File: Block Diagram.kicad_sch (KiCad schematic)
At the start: 0 parts

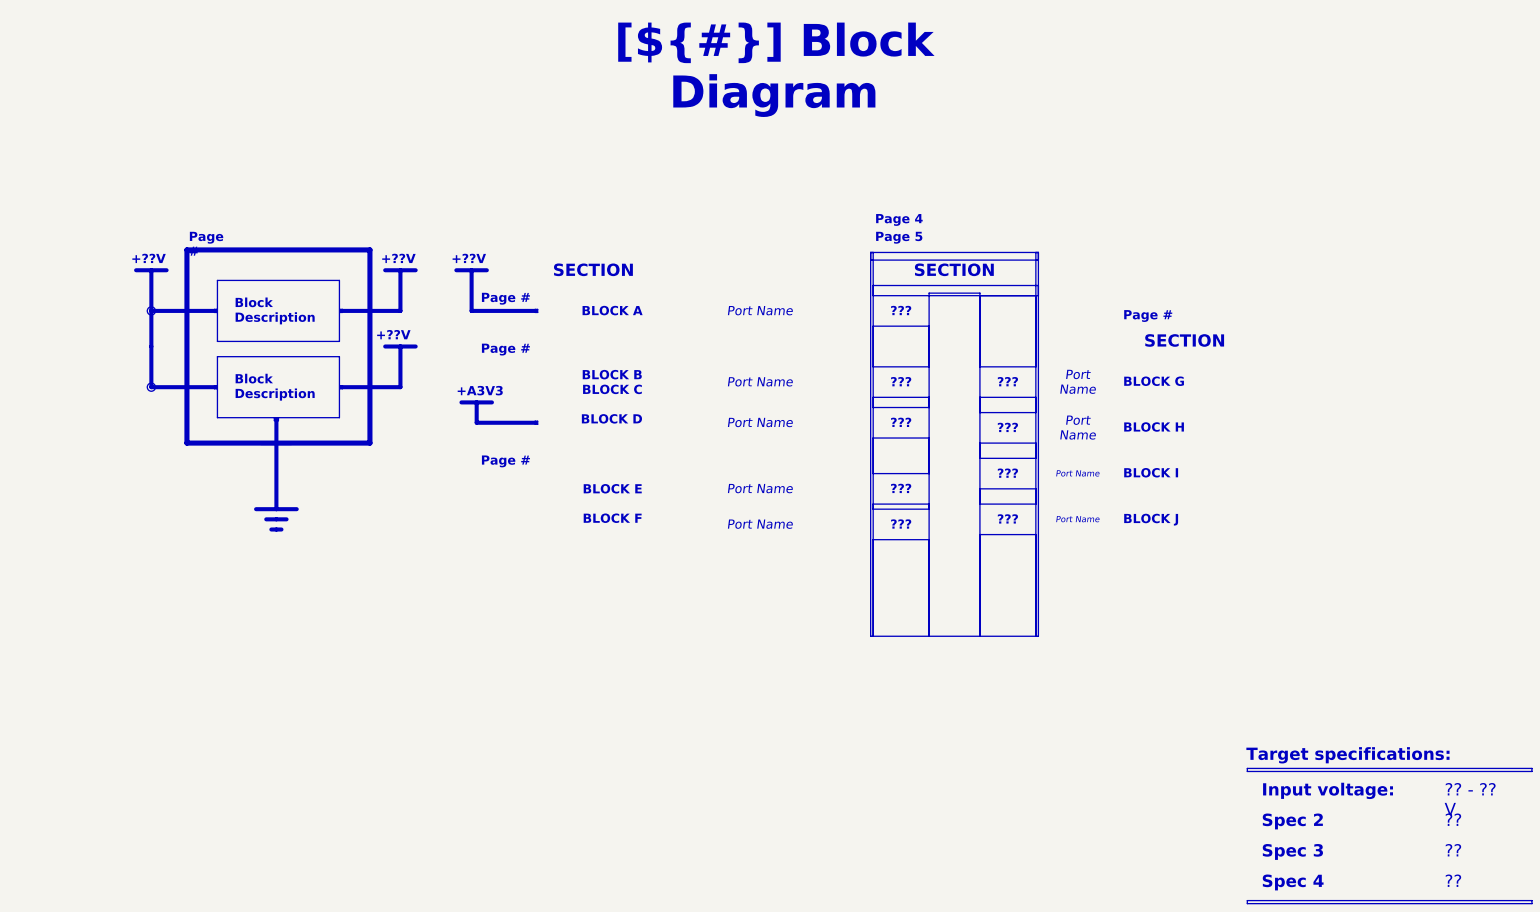
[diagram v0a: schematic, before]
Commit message: PCB[Grounding, Heat]: Added some more pours for heat considerations for bjt, stiched more vias for heat consideration on balanace resistors. SCH[Notes, Block Diagram]: Working on spelling and notes updates, started block diagram.
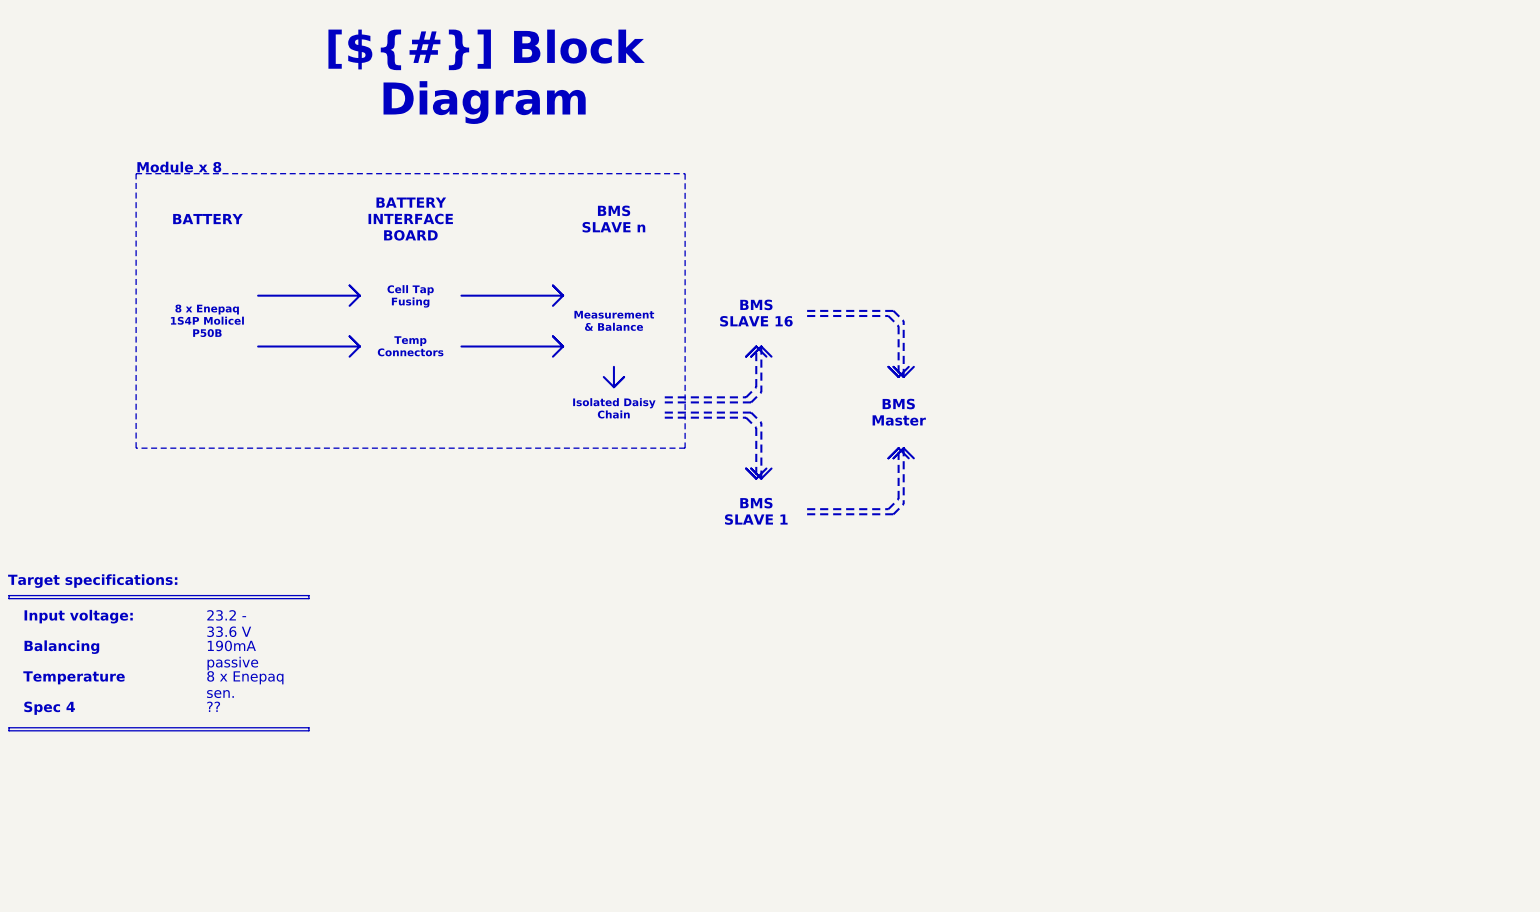
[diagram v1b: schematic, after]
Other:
- note added: "Module x 8"
- note removed: "+??V"
- note removed: "+A3V3"

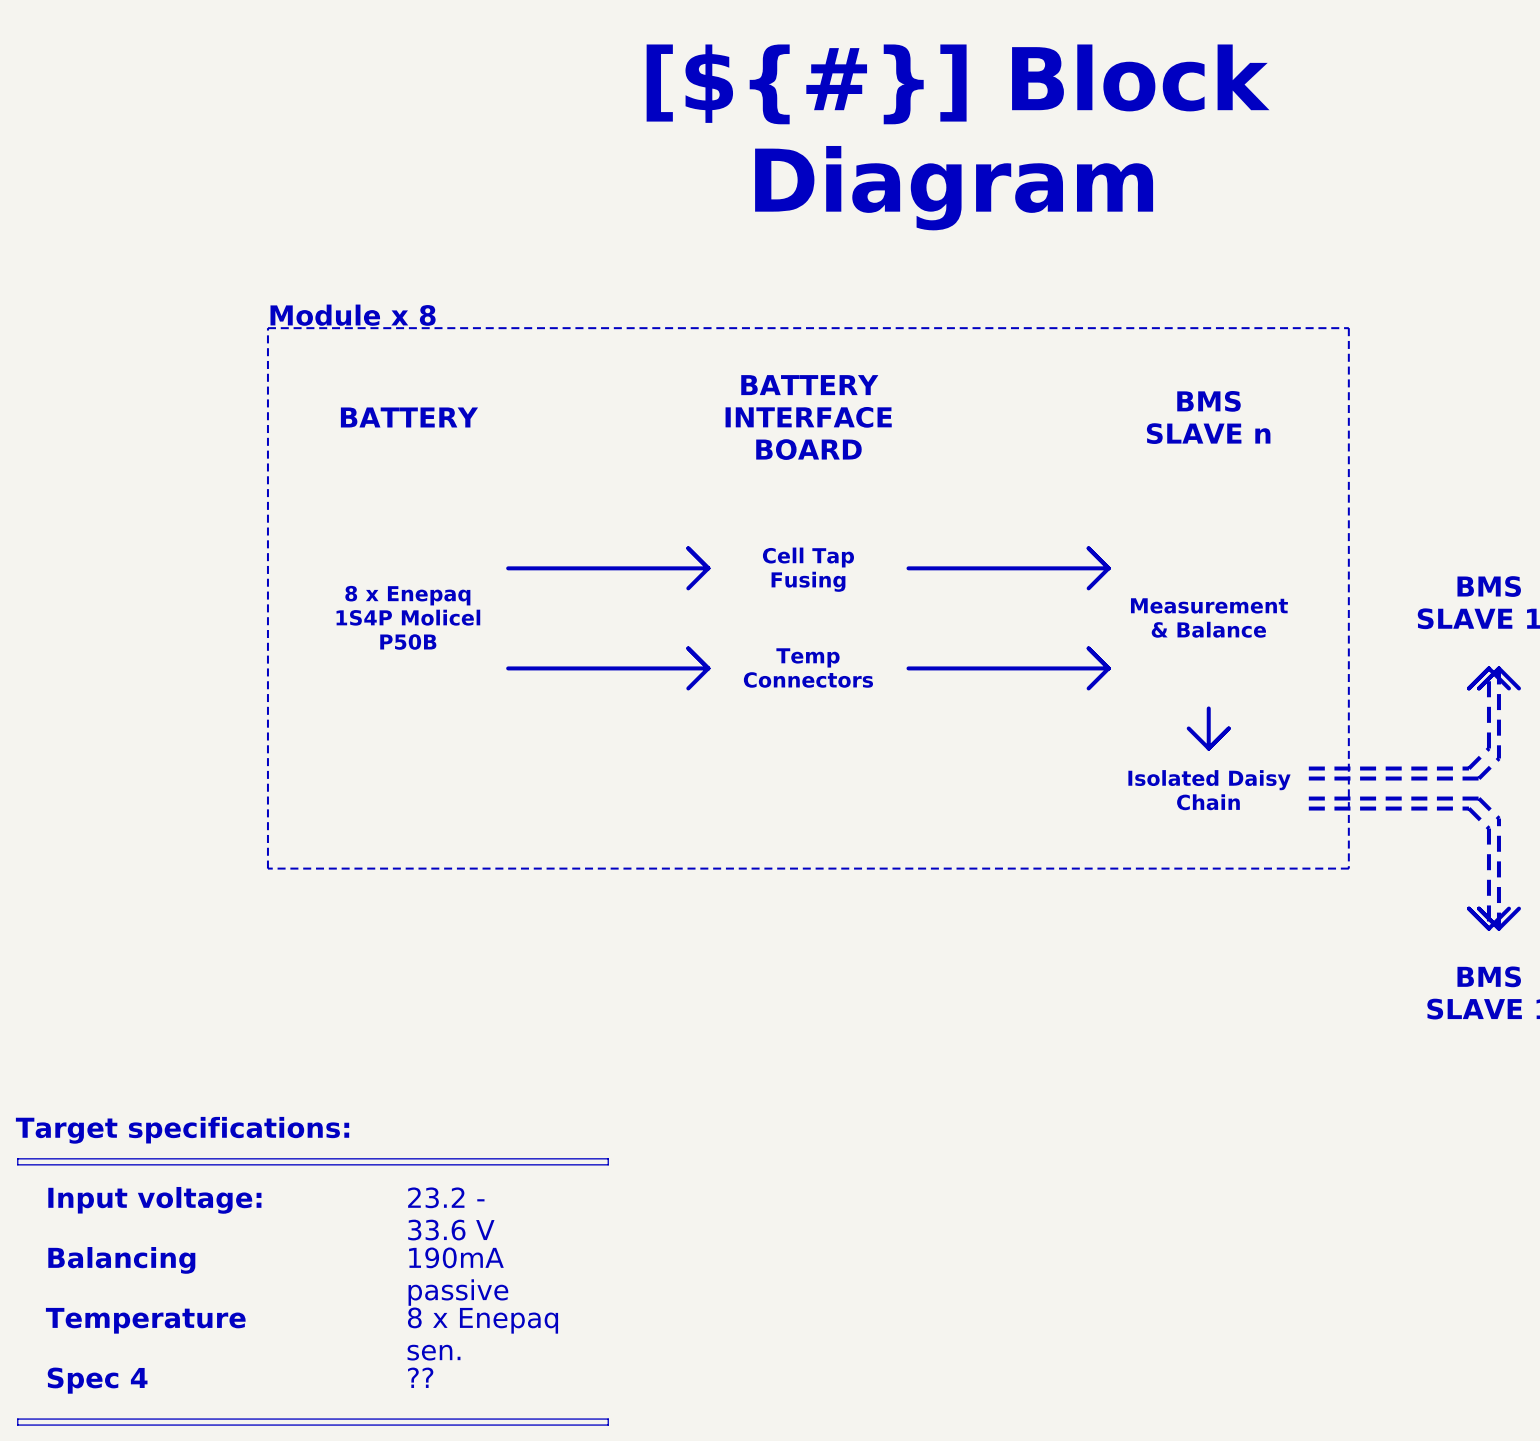
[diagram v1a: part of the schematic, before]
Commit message: PCB[Test Points, Mechanical, Silk]: Finalized Mounting Points, Added Testpoints with adjecent silkscreen labels. SCH[Test Points, Notes]: Added/Updated notes for all pages, cleaned up errors spelling ect.
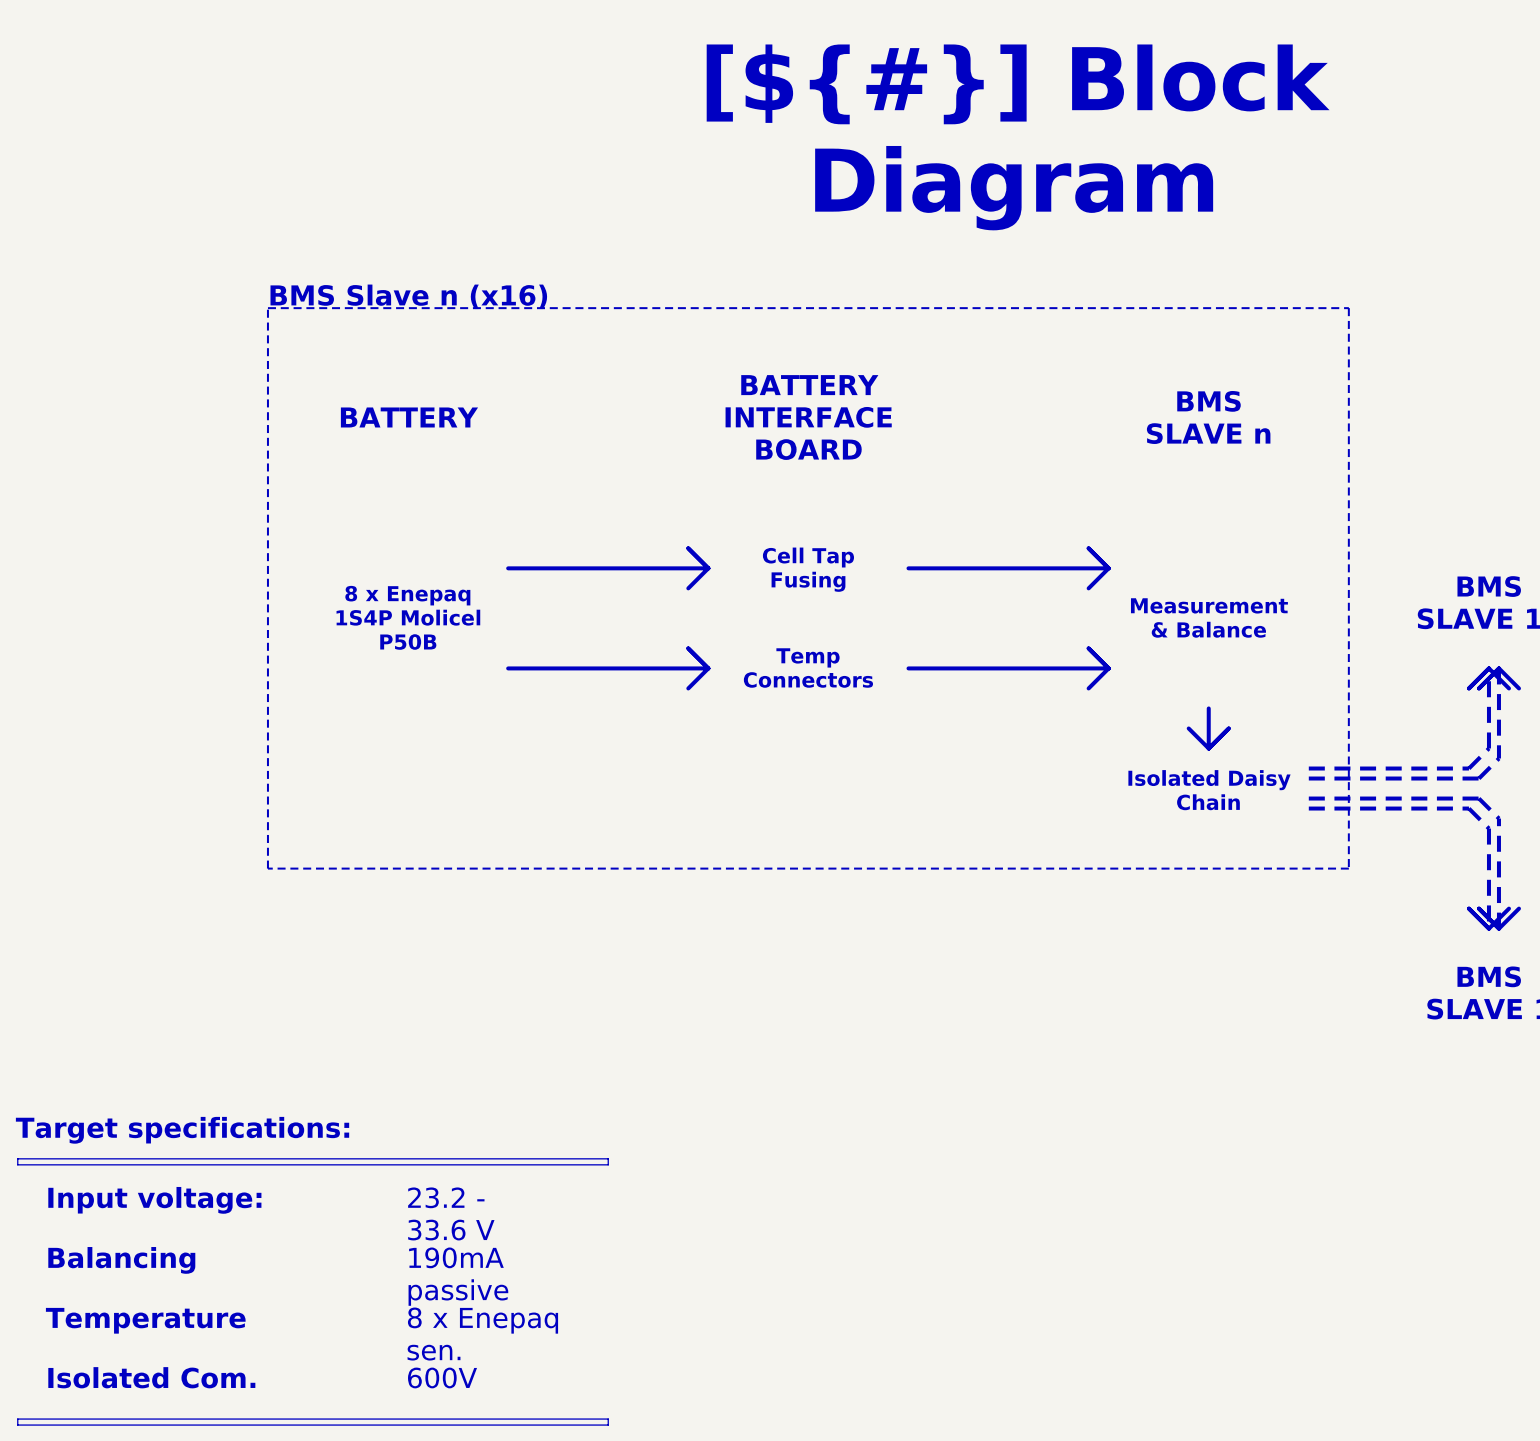
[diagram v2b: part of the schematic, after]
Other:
- note added: "BMS Slave n (x16)"
- note removed: "Module x 8"
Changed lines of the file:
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@@
 	)
 	(rectangle
-		(start 50.8 53.34)
+		(start 50.8 50.8)
 		(end 187.96 121.92)
 		(stroke
@@
 		)
 	)
-	(text "Module x 8"
-		(exclude_from_sim no)
-		(at 50.8 52.07 0)
+	(text "BMS Slave n (x16)"
+		(exclude_from_sim no)
+		(at 50.8 49.53 0)
 		(effects
 			(font
@@
 		)
 	)
-	(text_box "Spec 4"
+	(text_box "Isolated Com."
 		(exclude_from_sim no)
 		(at 20.32 182.88 0)
-		(size 44.45 7.62)
-		(margins 2.2859 2.2859 2.2859 2.2859)
-		(stroke
-			(width -0.0001)
-			(type default)
+		(size 44.45 8.5223)
+		(margins 2.2859 2.2859 2.2859 2.2859)
+		(stroke
+			(width -0.0001)
+			(type solid)
 		)
 		(fill
@@
 		)
 	)
-	(text_box "??"
+	(text_box "600V"
 		(exclude_from_sim no)
 		(at 66.04 182.88 0)
-		(size 27.94 7.62)
-		(margins 2.2859 2.2859 2.2859 2.2859)
-		(stroke
-			(width -0.0001)
-			(type default)
+		(size 27.94 8.5223)
+		(margins 2.2859 2.2859 2.2859 2.2859)
+		(stroke
+			(width -0.0001)
+			(type solid)
 		)
 		(fill
@@
 	(text_box "[${#}] ${TITLE}"
 		(exclude_from_sim no)
-		(at 72.39 16.1976 0)
+		(at 80.01 16.1976 0)
 		(size 130.81 24.4424)
 		(margins 5.9999 5.9999 5.9999 5.9999)
